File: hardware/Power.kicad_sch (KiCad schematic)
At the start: 76 parts, among them J5 Conn_01x02, J6 Conn_01x04, J7 Conn_01x02, J8 Conn_01x02, Q1 Q_NMOS, Q2 Q_NMOS, Q3 Q_NMOS, Q4 Q_NMOS, Q5 Q_PMOS, U5 BQ25798RQMR

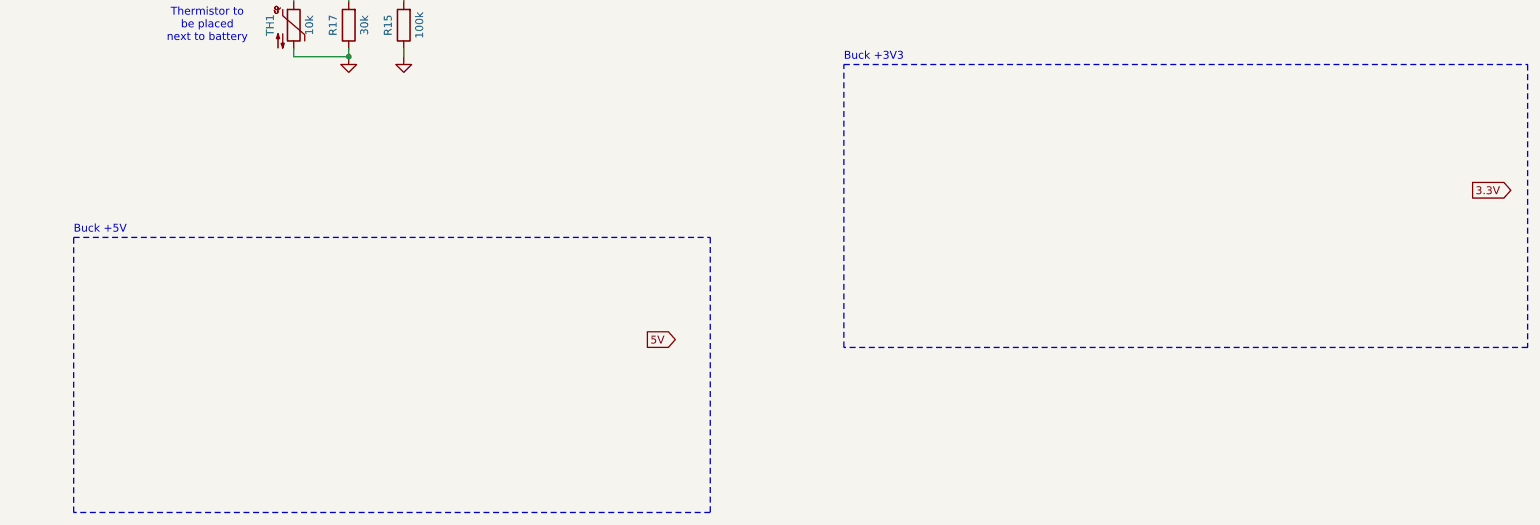
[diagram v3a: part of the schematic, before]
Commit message: Started 5V/3.3V buck & add components to lib
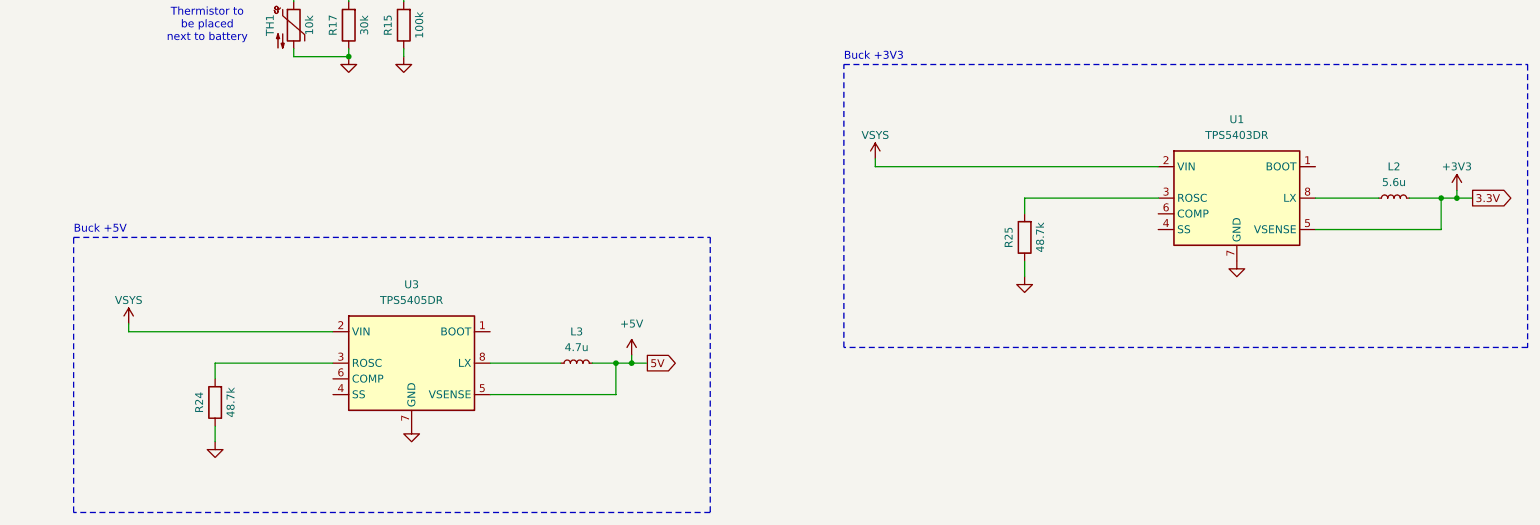
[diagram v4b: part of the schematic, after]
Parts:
- added L2: 5.6u, SRP4020TA-5R6M:IND_SRP4020TA-5R6M, symbol Device:L_Small
- added L3: 4.7u, Inductor_SMD:L_Sunlord_MWSA0412S, symbol Device:L_Small
- added R24, R25: 48.7k, Resistor_SMD:R_0402_1005Metric, symbol Device:R
- added U1: TPS5403DR, Package_SO:SOIC-8_3.9x4.9mm_P1.27mm, symbol Regulator_Switching:TPS5403
- added U3: TPS5405DR, Package_SO:SOIC-8_3.9x4.9mm_P1.27mm, symbol TPS5405:TPS5405DR
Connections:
- net 3.3V is gone; now on net +3V3: J6.3 (Pin_3)
- net +3V3: now also L2.2, U1.5 (VSENSE)
- net GND: now also R24.1, R25.1, U1.7 (GND), U3.7 (GND)
- net VSYS: now also U1.2 (VIN), U3.2 (VIN)
- net 5V renamed +5V
- net +5V: now also L3.2, U3.5 (VSENSE)
- new net: R25.2, U1.3 (ROSC)
- new net: L2.1, U1.8 (LX)
- new net: R24.2, U3.3 (ROSC)
- new net: L3.1, U3.8 (LX)

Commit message: Finished 3.3V/5V buck design
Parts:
- removed R24, R25: 48.7k, Resistor_SMD:R_0402_1005Metric, symbol Device:R
- removed U1: TPS5403DR, Package_SO:SOIC-8_3.9x4.9mm_P1.27mm, symbol Regulator_Switching:TPS5403
- removed U3: TPS5405DR, Package_SO:SOIC-8_3.9x4.9mm_P1.27mm, symbol TPS5405:TPS5405DR
- added C25, C29: 10u, Capacitor_SMD:C_0805_2012Metric, symbol Device:C_Small
- added C26, C27, C30, C31: 22u, Capacitor_SMD:C_0805_2012Metric, symbol Device:C_Small
- added C28, C32: 0.1u, Capacitor_SMD:C_0603_1608Metric, symbol Device:C_Small
- added TP27, TP28: TestPoint, symbol Connector:TestPoint
- added U1: AP63203WU, Package_TO_SOT_SMD:TSOT-23-6, symbol Regulator_Switching:AP63203WU
- added U3: AP63205WU, Package_TO_SOT_SMD:TSOT-23-6, symbol Regulator_Switching:AP63205WU
- L2: value 5.6u -> 3.9u
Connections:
- net +3V3: now also C26.1, C27.1, C28.2, U1.1 (FB)
- net +5V: now also C30.1, C31.1, C32.2, U3.1 (FB)
- net GND: now also C25.2, C26.2, C27.2, C29.2, C30.2, C31.2, U1.4 (GND), U3.4 (GND)
- net VSYS: now also C25.1, C29.1, U1.2 (EN), U1.3 (IN), U3.2 (EN), U3.3 (IN)
- net at L2.1: now also TP27.1, U1.5 (SW)
- net at L3.1: now also TP28.1, U3.5 (SW)
- new net: C28.1, U1.6 (BST)
- new net: C32.1, U3.6 (BST)
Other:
- note added: "Battery manager"
- moved on the sheet: C10, C11, C12, C13, C14, C15, C16, C17, C18, C19, C20, C21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

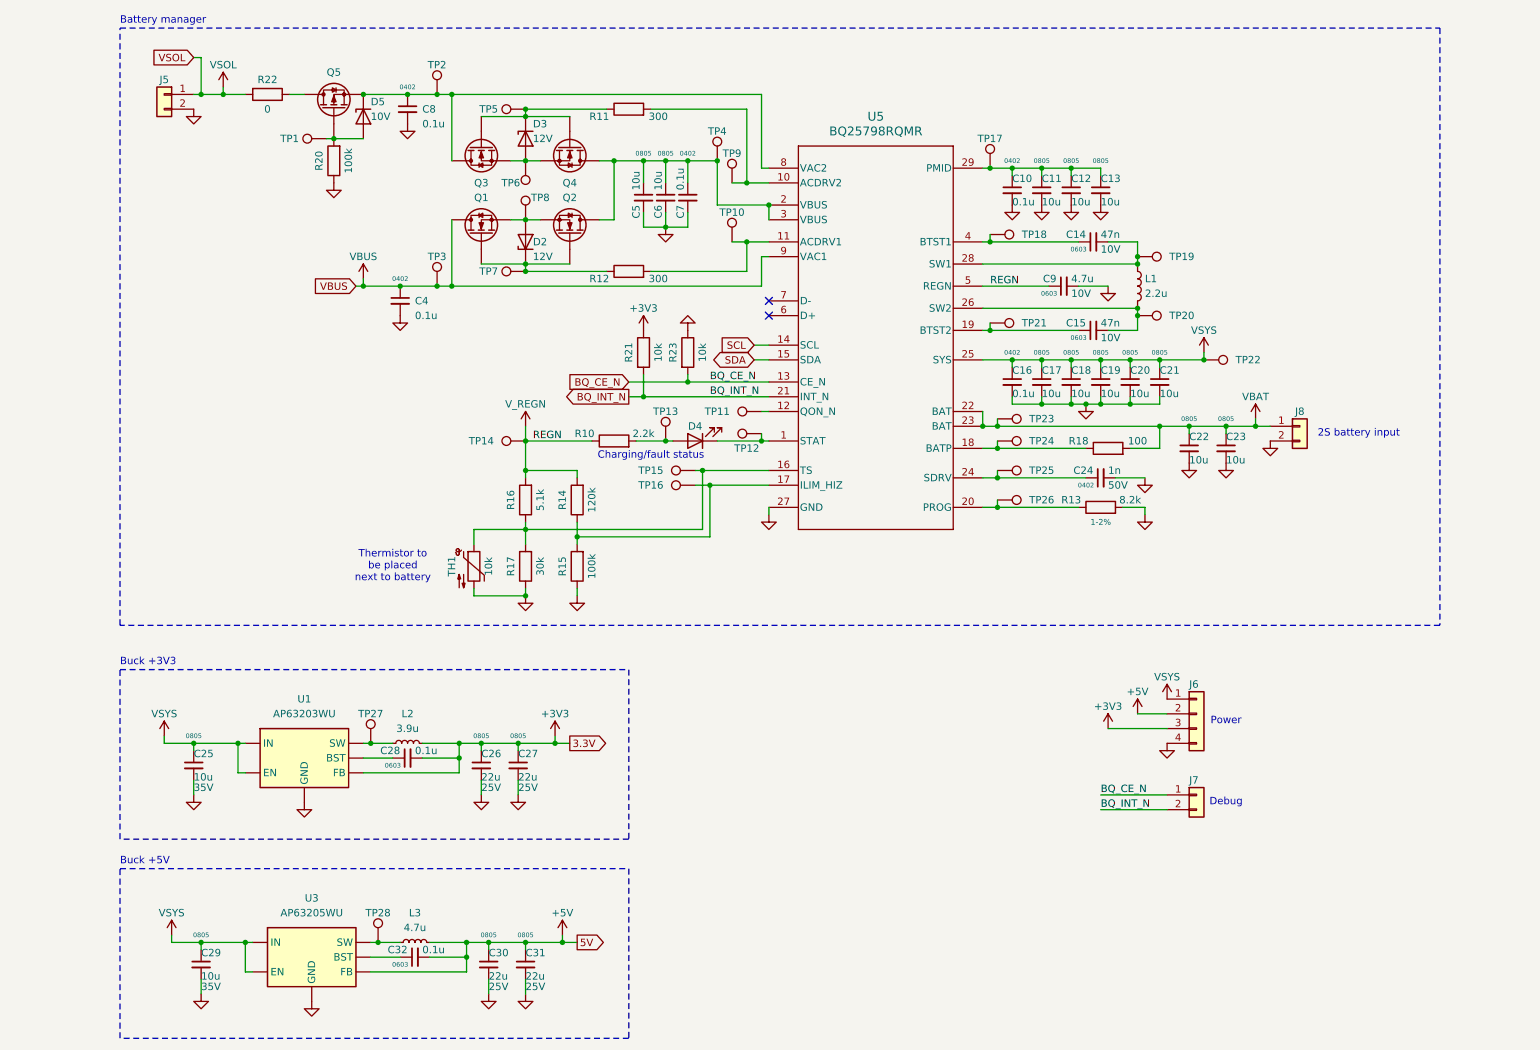
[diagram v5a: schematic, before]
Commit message: Found all capacitors & inductors footprint & JLCPCB
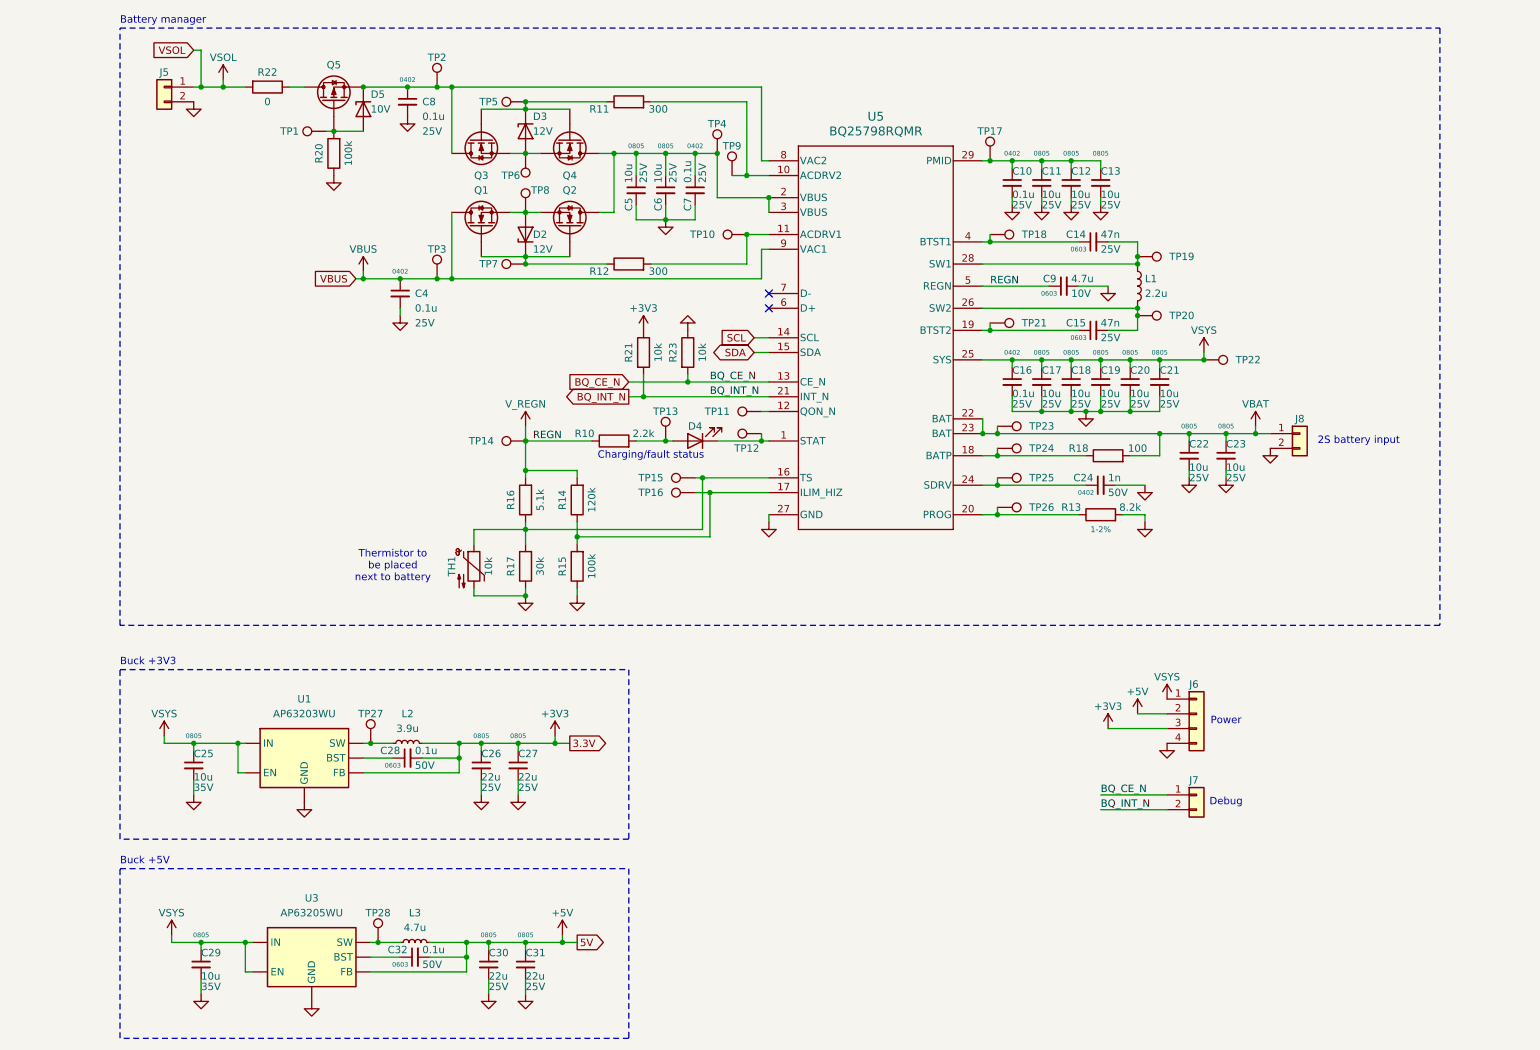
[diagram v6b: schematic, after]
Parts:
- C10, C16, C4, C7, C8: JLCPCB Part # (none) -> C100072; Voltage (none) -> 25V
- C11, C12, C13, C17, C18, C19, C20, C21, C22, C23, C5, C6: JLCPCB Part # (none) -> C15850; Voltage (none) -> 25V
- C14, C15: JLCPCB Part # (none) -> C113811; Voltage 10V -> 25V
- C24: JLCPCB Part # (none) -> C14442
- C25, C29: JLCPCB Part # (none) -> C33546007
- C26, C27, C30, C31: JLCPCB Part # (none) -> C45783
- C28, C32: JLCPCB Part # (none) -> C14663; Voltage (none) -> 50V
- C9: JLCPCB Part # (none) -> C1705
- L1: JLCPCB Part # (none) -> C2847475; Package (none) -> SMD, 5.7x5.2mm
- L2: footprint SRP4020TA-5R6M:IND_SRP4020TA-5R6M -> Inductor_SMD:L_Sunlord_SWPA4030S; Availability In Stock -> (none); JLCPCB Part # (none) -> C96899; MANUFACTURER Bourns -> (none); MF Bourns -> (none); MP SRP4020TA-5R6M -> (none); Package SMD-2 Bourns -> SMD, 4x4mm; STANDARD Manufacturer Recommendation -> (none); SnapEDA_Link https://www.snapeda.com/parts/SRP4020TA-5R6M/Bourns/view-pa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 -> (none)
- L3: footprint Inductor_SMD:L_Sunlord_MWSA0412S -> Inductor_SMD:L_Sunlord_SWPA4030S; JLCPCB Part # (none) -> C57269; Package (none) -> SMD, 4x4mm
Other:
- moved on the sheet: C10, C11, C12, C13, C22, C23, C24, C4, C5, C6, C7, C8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

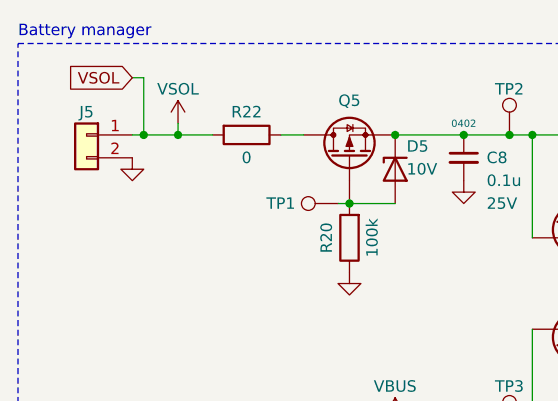
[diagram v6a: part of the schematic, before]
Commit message: Found all resistors & pin headers footprint & JLCPCB
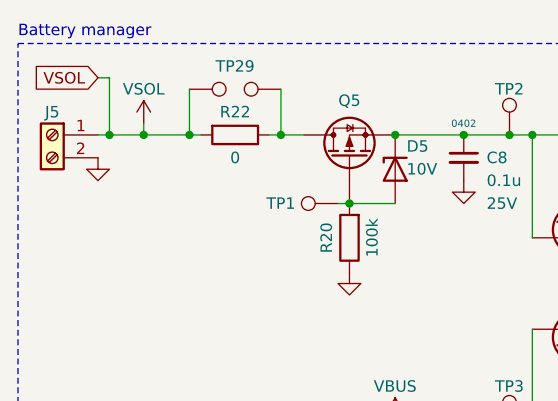
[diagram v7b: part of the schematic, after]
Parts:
- added TP29: TestPoint_2Pole, Connector_PinHeader_2.54mm:PinHeader_2x01_P2.54mm_Vertical, symbol Connector:TestPoint_2Pole
- J5: value Conn_01x02 -> Screw_Terminal_01x02; footprint (none) -> GoG_Library:TerminalBlock_WJ126V-5.0-2P_1x02_P5.00mm; symbol Connector_Generic:Conn_01x02 -> Connector:Screw_Terminal_01x02; JLCPCB Part # (none) -> C8404; Package (none) -> Plugin,P=5mm
- J6: footprint (none) -> Connector_PinHeader_2.54mm:PinHeader_1x04_P2.54mm_Vertical; JLCPCB Part # (none) -> C7501262; Package (none) -> Plugin,P=2.54mm
- J7: footprint (none) -> Connector_PinHeader_2.54mm:PinHeader_1x02_P2.54mm_Vertical; JLCPCB Part # (none) -> C7501260; Package (none) -> Plugin,P=2.54mm
- R10: JLCPCB Part # (none) -> C163447; Package (none) -> 0402
- R11, R12: footprint Resistor_SMD:R_0402_1005Metric -> Resistor_SMD:R_0603_1608Metric; JLCPCB Part # (none) -> C114617; Package (none) -> 0603
- R13: JLCPCB Part # (none) -> C137929; Package (none) -> 0402
- R14: JLCPCB Part # (none) -> C93945; Package (none) -> 0402
- R15, R20: JLCPCB Part # (none) -> C60491; Package (none) -> 0402
- R16: JLCPCB Part # (none) -> C105872; Package (none) -> 0402
- R17: JLCPCB Part # (none) -> C138008; Package (none) -> 0402
- R18: JLCPCB Part # (none) -> C106232; Package (none) -> 0402
- R21, R23: JLCPCB Part # (none) -> C60490; Package (none) -> 0402
- R22: footprint Resistor_SMD:R_0402_1005Metric -> Resistor_SMD:R_1206_3216Metric; JLCPCB Part # (none) -> C7467250; Package (none) -> 1206
- U1: JLCPCB Part # (none) -> C780769; Package (none) -> TSOT-23-6
- U3: JLCPCB Part # (none) -> C2071056; Package (none) -> TSOT-23-6
- U5: JLCPCB Part # (none) -> C2876593; Package (none) -> QFN-29(4x4)
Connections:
- net VSOL: now also TP29.1
- net at Q5.D, R22.1: now also TP29.2
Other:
- moved on the sheet: R22

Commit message: Found all diodes & transistors footprint & JLCPCB
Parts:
- D2, D3: JLCPCB Part # (none) -> C97772; Package (none) -> SOD-123
- D4: JLCPCB Part # (none) -> C7470862; Package (none) -> 0603
- D5: JLCPCB Part # (none) -> C48870; Package (none) -> SOD-123
- J8: footprint (none) -> Connector_JST:JST_XH_B2B-XH-A_1x02_P2.50mm_Vertical; JLCPCB Part # (none) -> C158012; Package (none) -> Plugin,P=2.5mm
- Q1, Q2, Q3, Q4: footprint (none) -> Package_TO_SOT_SMD:SOT-23; JLCPCB Part # (none) -> C2938367; Package (none) -> SOT-23
- Q5: footprint (none) -> Package_TO_SOT_SMD:SOT-23; JLCPCB Part # (none) -> C5350989; Package (none) -> SOT-23
- TH1: JLCPCB Part # (none) -> -; Package (none) -> -
- TP1, TP10, TP11, TP12, TP13, TP14, TP15, TP16, TP17, TP18, TP19, TP2, TP20, TP21, TP22, TP23, TP24, TP25, TP26, TP27, TP28, TP3, TP4, TP5, TP6, TP7, TP8, TP9: footprint (none) -> TestPoint:TestPoint_Pad_D1.5mm
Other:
- company: ECAM -> ECAM Brussels Engineering School
